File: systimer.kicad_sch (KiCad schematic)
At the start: 8 parts, among them SW3 timersw, U33 74HC541, U7 74HC14

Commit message: done the pcb layout + added the 1M ram bank project
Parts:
- C7, C8: footprint Capacitor_THT:C_Disc_P2.54mm -> Capacitor_THT:C_Disc_D3.0mm_W1.6mm_P2.54mm
- U33: footprint Package_DIP:DIP-20_W7.62mm_Socket -> Package_DIP:DIP-20_W7.62mm
- U7: footprint Package_DIP:DIP-14_W7.62mm_Socket -> Package_DIP:DIP-14_W7.62mm
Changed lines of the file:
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@@
 			)
 		)
-		(property "Footprint" "Package_DIP:DIP-20_W7.62mm_Socket"
+		(property "Footprint" "Package_DIP:DIP-20_W7.62mm"
 			(at 165.1 91.44 0)
 			(effects
@@
 			)
 		)
-		(property "Footprint" "Package_DIP:DIP-14_W7.62mm_Socket"
+		(property "Footprint" "Package_DIP:DIP-14_W7.62mm"
 			(at 119.38 101.6 0)
 			(effects
@@
 			)
 		)
-		(property "Footprint" "Capacitor_THT:C_Disc_P2.54mm"
+		(property "Footprint" "Capacitor_THT:C_Disc_D3.0mm_W1.6mm_P2.54mm"
 			(at 139.7 100.6348 0)
 			(effects
@@
 			)
 		)
-		(property "Footprint" "Capacitor_THT:C_Disc_P2.54mm"
+		(property "Footprint" "Capacitor_THT:C_Disc_D3.0mm_W1.6mm_P2.54mm"
 			(at 110.7948 114.3 0)
 			(effects

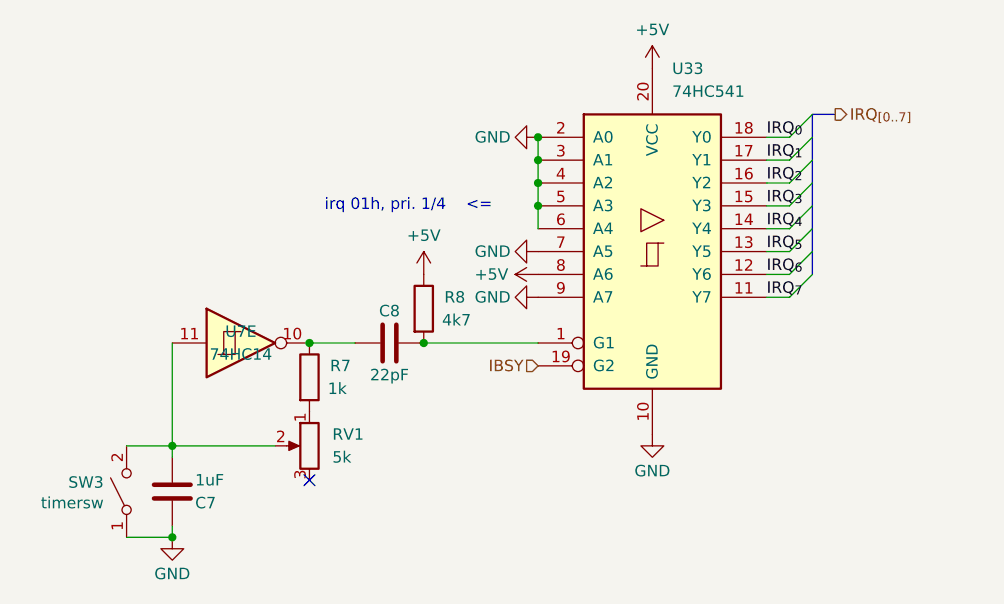
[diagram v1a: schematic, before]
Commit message: first commit: scheme ok [decoder]: 	- new spv. address space [mmu]: 	- removed pidreg 	- switched back to 8Kb mmu rams [ram/peripherals]: 	- added ground pins to connectors [misc]: 	- added DMA support 	- added clock halfer
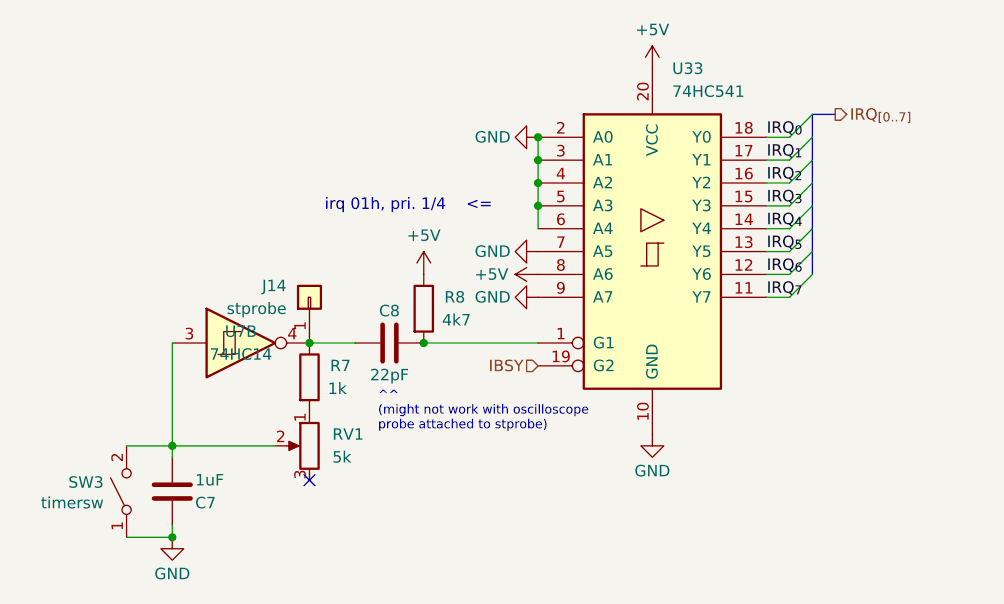
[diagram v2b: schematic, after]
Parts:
- removed U7: 74HC14, Package_DIP:DIP-14_W7.62mm, symbol 74xx:74HC14
- added J14: stprobe, symbol Connector_Generic:Conn_01x01
- added U7: 74HC14, Package_DIP:DIP-14_W7.62mm, symbol 74xx:74HC14
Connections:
- net at C8.1, R7.1: now also J14.1 (Pin_1), U7.4
- net at C7.2, RV1.2, SW3.2 (B): now also U7.3
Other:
- note added: "^^ (might not work with oscilloscope probe attached to stprobe)"
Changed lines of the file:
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@@
 	(generator_version "9.0")
 	(paper "A4")
+	(text "^^\n(might not work with oscilloscope\nprobe attached to stprobe)"
+		(exclude_from_sim no)
+		(at 134.62 109.22 0)
+		(effects
+			(font
+				(size 1.016 1.016)
+			)
+			(justify left)
+		)
+	)
 	(text "irq 01h, pri. 1/4	<="
 		(exclude_from_sim no)
@@
 	)
 	(symbol
+		(lib_id "power:GND")
+		(at 152.4 91.44 270)
+		(unit 1)
+		(exclude_from_sim no)
+		(in_bom yes)
+		(on_board yes)
+		(dnp no)
+		(property "Reference" "#PWR091"
+			(at 146.05 91.44 0)
+			(effects
+				(font
+					(size 1.27 1.27)
+				)
+				(hide yes)
+			)
+		)
+		(property "Value" "GND"
+			(at 149.352 91.44 90)
+			(effects
+				(font
+					(size 1.27 1.27)
+				)
+				(justify right)
+			)
+		)
+		(property "Footprint" ""
+			(at 152.4 91.44 0)
+			(effects
+				(font
+					(size 1.27 1.27)
+				)
+				(hide yes)
+			)
+		)
+		(property "Datasheet" ""
+			(at 152.4 91.44 0)
+			(effects
+				(font
+					(size 1.27 1.27)
+				)
+				(hide yes)
+			)
+		)
+		(property "Description" "Power symbol creates a global label with name \"GND\" , ground"
+			(at 152.4 91.44 0)
+			(effects
+				(font
+					(size 1.27 1.27)
+				)
+				(hide yes)
+			)
+		)
+		(pin "1"
+		)
+		(instances
+			(project "SCRM6816"
+				(path "/56448118-82b3-4e1c-bda3-84d63e01a14a/6370f5b1-3859-4547-885f-6a592ab59011"
+					(reference "#PWR091")
+					(unit 1)
+				)
+			)
+		)
+	)
+	(symbol
 		(lib_id "74xx:74HC14")
 		(at 119.38 101.6 0)
-		(unit 5)
+		(unit 2)
 		(exclude_from_sim no)
 		(in_bom yes)
@@
 				(path "/56448118-82b3-4e1c-bda3-84d63e01a14a/6370f5b1-3859-4547-885f-6a592ab59011"
 					(reference "U7")
-					(unit 5)
-				)
-			)
-		)
-	)
-	(symbol
-		(lib_id "power:GND")
-		(at 152.4 91.44 270)
-		(unit 1)
-		(exclude_from_sim no)
-		(in_bom yes)
-		(on_board yes)
-		(dnp no)
-		(property "Reference" "#PWR091"
-			(at 146.05 91.44 0)
-			(effects
-				(font
-					(size 1.27 1.27)
-				)
-				(hide yes)
-			)
-		)
-		(property "Value" "GND"
-			(at 149.352 91.44 90)
-			(effects
-				(font
-					(size 1.27 1.27)
-				)
-				(justify right)
-			)
-		)
-		(property "Footprint" ""
-			(at 152.4 91.44 0)
-			(effects
-				(font
-					(size 1.27 1.27)
-				)
-				(hide yes)
-			)
-		)
-		(property "Datasheet" ""
-			(at 152.4 91.44 0)
-			(effects
-				(font
-					(size 1.27 1.27)
-				)
-				(hide yes)
-			)
-		)
-		(property "Description" "Power symbol creates a global label with name \"GND\" , ground"
-			(at 152.4 91.44 0)
-			(effects
-				(font
-					(size 1.27 1.27)
-				)
-				(hide yes)
-			)
-		)
-		(pin "1"
-		)
-		(instances
-			(project "SCRM6816"
-				(path "/56448118-82b3-4e1c-bda3-84d63e01a14a/6370f5b1-3859-4547-885f-6a592ab59011"
-					(reference "#PWR091")
-					(unit 1)
+					(unit 2)
 				)
 			)
@@
 					(unit 1)
 				)
+			)
+		)
+	)
+	(symbol
+		(lib_id "Connector_Generic:Conn_01x01")
+		(at 127 96.52 90)
+		(unit 1)
+		(exclude_from_sim no)
+		(in_bom yes)
+		(on_board yes)
+		(dnp no)
+		(property "Reference" "J14"
+			(at 124.46 95.2499 90)
+			(effects
+				(font
+					(size 1.27 1.27)
+				)
+				(justify left)
+			)
+		)
+		(property "Value" "stprobe"
+			(at 124.46 97.7899 90)
+			(effects
+				(font
+					(size 1.27 1.27)
+				)
+				(justify left)
+			)
+		)
+		(property "Footprint" ""
+			(at 127 96.52 0)
+			(effects
+				(font
+					(size 1.27 1.27)
+				)
+				(hide yes)
+			)
+		)
+		(property "Datasheet" "~"
+			(at 127 96.52 0)
+			(effects
+				(font
+					(size 1.27 1.27)
+				)
+				(hide yes)
+			)
+		)
+		(property "Description" "Generic connector, single row, 01x01, script generated (kicad-library-utils/schlib/autogen/connector/)"
+			(at 127 96.52 0)
+			(effects
+				(font
+					(size 1.27 1.27)
+				)
+				(hide yes)
+			)
+		)
+		(pin "1"
+		)
+		(instances
+			(project ""
+				(path "/56448118-82b3-4e1c-bda3-84d63e01a14a/6370f5b1-3859-4547-885f-6a592ab59011"
+					(reference "J14")
+					(unit 1)
+				)
